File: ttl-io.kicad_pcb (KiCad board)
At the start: 4 copper layers, 47.2 x 30 mm, 56 parts, among them J1 PMOD, J2 430451628, U1 SN74LVC1G16DBVR, U2 SN74LVC1G16DBVR, U3 SN74LVC1G16DBVR, U4 SN74LVC1G16DBVR, U5 SN74AC14PWR, U6 SN74LVC3G34DCT, U7 SN74LVC3G34DCT, U8 SN74LVC3G34DCT, U9 SN74LVC3G34DCT

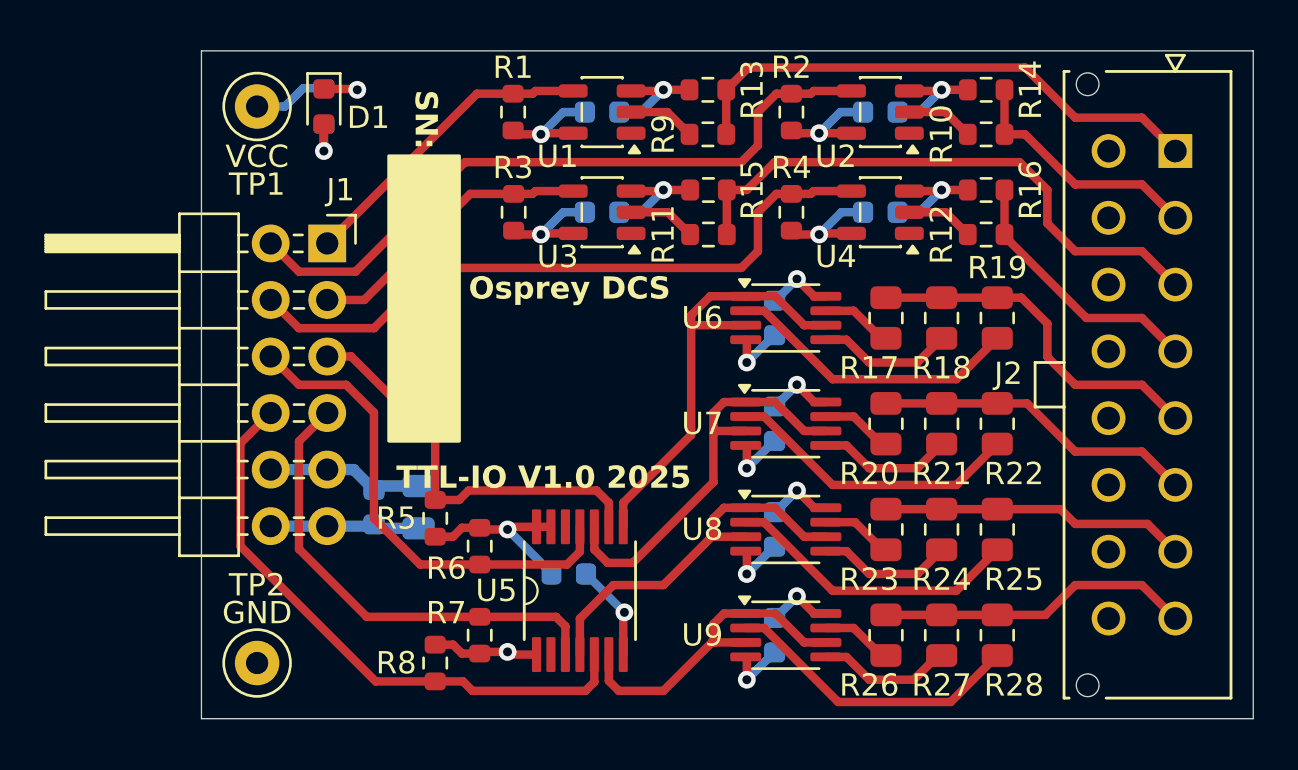
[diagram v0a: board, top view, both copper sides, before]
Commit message: pcb tweaks, date/ver, U5 3D model, 0.4mm holes
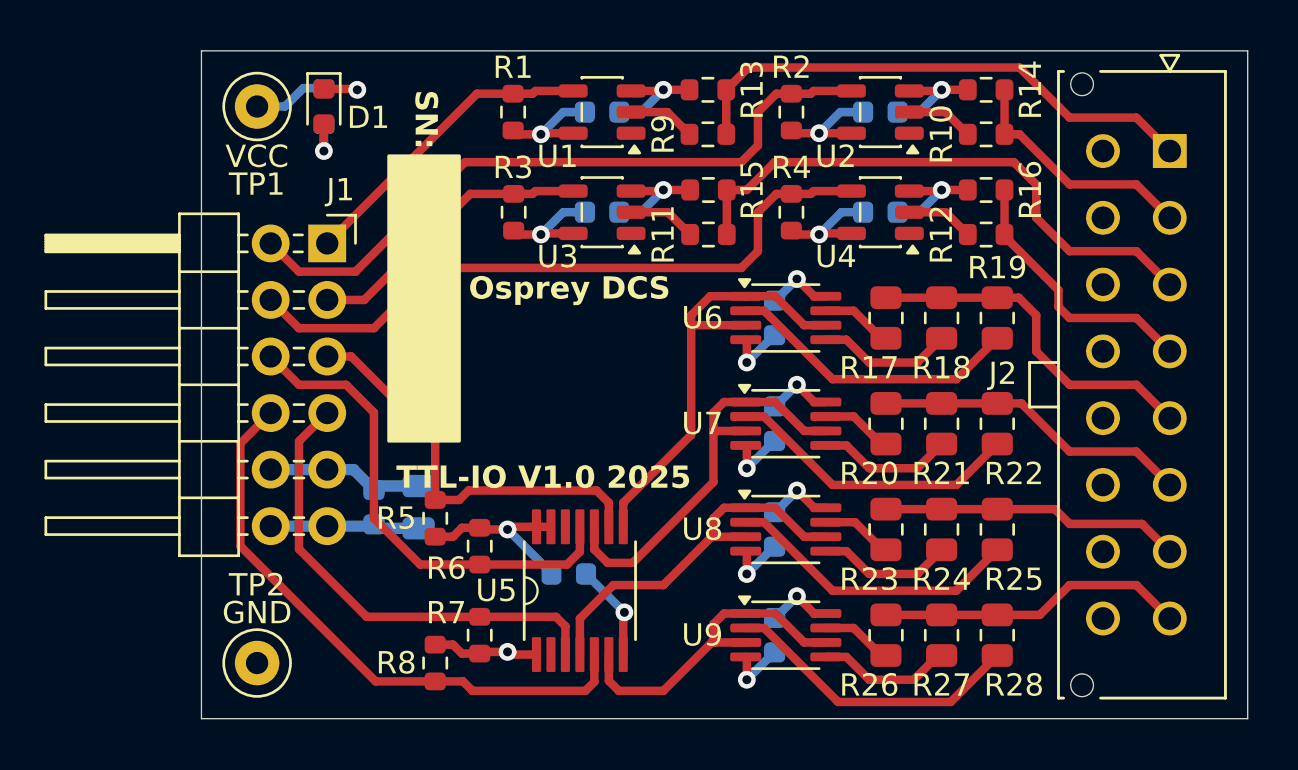
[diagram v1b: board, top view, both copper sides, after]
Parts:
- moved J2 0.25 mm to (169.5, 85.0)
- moved Logo1 0.25 mm to (160.9, 85.6)
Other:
- board size 47.2 x 30 mm -> 47 x 30 mm

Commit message: 30x35mm version initial commit
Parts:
- removed J2: 430451628, 0local:430451628
- removed the R17 at (158.2, 82.0)
- removed the R18 at (160.8, 82.0)
- removed the R19 at (163.2, 82.0)
- removed the R20 at (158.2, 86.8)
- removed the R21 at (160.8, 86.8)
- removed the R22 at (163.2, 86.8)
- removed the R23 at (158.2, 91.5)
- removed the R24 at (160.8, 91.5)
- removed the R25 at (163.2, 91.5)
- removed the R26 at (158.2, 96.2)
- removed the R27 at (160.8, 96.2)
- removed the R28 at (163.2, 96.2)
- added I1: MMCX, 0local:MMCX_THT_Vertical, F.Cu at (154.2, 72.8)
- added I2: MMCX, 0local:MMCX_THT_Vertical, F.Cu at (154.2, 79.8)
- added I3: MMCX, 0local:MMCX_THT_Vertical, F.Cu at (154.2, 86.7)
- added I4: MMCX, 0local:MMCX_THT_Vertical, F.Cu at (154.2, 93.8)
- added O1: MMCX, 0local:MMCX_THT_Vertical, F.Cu at (159.8, 76.2)
- added O2: MMCX, 0local:MMCX_THT_Vertical, F.Cu at (159.8, 83.2)
- added O3: MMCX, 0local:MMCX_THT_Vertical, F.Cu at (159.8, 90.2)
- added O4: MMCX, 0local:MMCX_THT_Vertical, F.Cu at (159.8, 97.2)
- added R10: 10, 0local:R_0805_2012Metric, F.Cu at (149.8, 81.2)
- added R11: 10, 0local:R_0805_2012Metric, F.Cu at (149.8, 88.8)
- added R12: 10, 0local:R_0805_2012Metric, F.Cu at (149.8, 90.8)
- added R13: 10, 0local:R_0805_2012Metric, F.Cu at (149.8, 92.8)
- added R14: 10, 0local:R_0805_2012Metric, F.Cu at (149.8, 94.8)
- added R15: 10, 0local:R_0805_2012Metric, F.Cu at (149.8, 96.8)
- added R16: 10, 0local:R_0805_2012Metric, F.Cu at (149.8, 98.8)
- added R5: 10, 0local:R_0805_2012Metric, F.Cu at (149.8, 71.2)
- added R6: 10, 0local:R_0805_2012Metric, F.Cu at (149.8, 73.2)
- added R7: 10, 0local:R_0805_2012Metric, F.Cu at (149.8, 75.2)
- added R8: 10, 0local:R_0805_2012Metric, F.Cu at (149.8, 77.2)
- added R9: 10, 0local:R_0805_2012Metric, F.Cu at (149.8, 79.2)
- C1, C2, C3, C4: moved to F.Cu
- R17: renamed from R13; moved to B.Cu
- R18: renamed from R14; moved to B.Cu
- R19: renamed from R15; moved to B.Cu
- R20: renamed from R16; moved to B.Cu
- R21: renamed from R9; moved to B.Cu
- R22: renamed from R10; moved to B.Cu
- R23: renamed from R11; moved to B.Cu
- R24: renamed from R12; moved to B.Cu
- R25: renamed from R1; moved to B.Cu
- R26: renamed from R2; moved to B.Cu
- R27: renamed from R3; moved to B.Cu
- R28: renamed from R4; moved to B.Cu
- U6: renamed from U1; moved to B.Cu
- U7: renamed from U2; moved to B.Cu
- U8: renamed from U3; moved to B.Cu
- U9: renamed from U4; moved to B.Cu
- moved C4 27.2 mm to (139.2, 97.0), turned to 90 degrees
- moved U9 27.2 mm to (139.2, 97.0)
- moved R28 26.7 mm to (136.0, 97.0), turned to -90 degrees
- moved R20 21.7 mm to (151.0, 94.5), turned to 90 degrees
- moved R24 21.2 mm to (148.2, 93.8)
- moved C2 19.3 mm to (139.2, 77.5), turned to 90 degrees
- moved U7 19.3 mm to (139.2, 77.5)
- moved R26 18.6 mm to (136.0, 77.5), turned to -90 degrees
- moved R27 17.5 mm to (135.0, 93.5), turned to 0 degrees
- moved C3 16.5 mm to (139.2, 92.5), turned to 90 degrees
- moved U8 16.5 mm to (139.2, 92.5)
- moved R22 15.7 mm to (148.2, 79.8)
- moved C9 15.3 mm to (136.8, 80.0)
- moved R19 14.8 mm to (155.0, 90.2), turned to 180 degrees
- moved R18 13.8 mm to (151.0, 79.0), turned to -90 degrees
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- renumbered C6 to C5, C7 to C6, C8 to C7, C9 to C8, C5 to C9, R5 to R1, R6 to R2, R7 to R3, R8 to R4, U5 to U1, U6 to U2, U7 to U3, U8 to U4, U9 to U5
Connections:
- U1 pad 1: +3.3V -> /PMOD_OUT4
- U1 pad 10: Net-(U5-5Y) -> Net-(U1-5Y)
- U1 pad 11: /PMOD_OUT2 -> /PMOD_OUT1
- U1 pad 2: unconnected-(U5-1Y-Pad2) -> Net-(U1-1Y)
- U1 pad 3: /PMOD_OUT3 -> +3.3V
- U1 pad 4: Net-(U5-2Y) (its old number) -> unconnected-(U1-2Y-Pad4)
- U1 pad 5: /PMOD_OUT4 -> /PMOD_OUT3
- U1 pad 6: Net-(U5-3Y) (its old number) -> Net-(U1-3Y)
- U1 pad 8: Net-(U5-4Y) -> Net-(U1-4Y)
- U1 pad 9: /PMOD_OUT1 -> /PMOD_OUT2
- U2 pad 1: Net-(U5-4Y) -> Net-(U1-5Y)
- U2 pad 3: Net-(U5-4Y) -> Net-(U1-5Y)
- U2 pad 6: Net-(U5-4Y) -> Net-(U1-5Y)
- U3 pad 1: Net-(U5-5Y) -> Net-(U1-4Y)
- U3 pad 3: Net-(U5-5Y) -> Net-(U1-4Y)
- U3 pad 6: Net-(U5-5Y) -> Net-(U1-4Y)
- U4 pad 1: Net-(U5-2Y) (its old number) -> Net-(U1-3Y)
- U4 pad 3: Net-(U5-2Y) (its old number) -> Net-(U1-3Y)
- U4 pad 6: Net-(U5-2Y) (its old number) -> Net-(U1-3Y)
- U5 pad 1: Net-(U5-3Y) (its old number) -> Net-(U1-1Y)
- U5 pad 3: Net-(U5-3Y) (its old number) -> Net-(U1-1Y)
- U5 pad 6: Net-(U5-3Y) (its old number) -> Net-(U1-1Y)
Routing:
- net /PMOD_IN2: track 30.9 -> 8.59 mm
- net /IN3: track 25.6 -> 5.14 mm
- net Net-(U5-4Y): track 20.2 -> 0.00 mm
- net /IN1: track 23.9 -> 5.24 mm
- net Net-(U5-5Y): track 18.5 -> 0.00 mm
- net Net-(U1-5Y): track 0.00 -> 18.3 mm
- net Net-(U1-1Y): track 0.00 -> 18.0 mm
- net /PMOD_OUT4: track 26.5 -> 8.82 mm
- net Net-(U5-2Y) (its old number): track 17.1 -> 0.00 mm
- net Net-(U5-3Y) (its old number): track 15.1 -> 0.00 mm
- net Net-(U1-4Y): track 0.00 -> 12.3 mm
- net Net-(U1-3Y): track 0.00 -> 12.0 mm
- net /PMOD_OUT1: track 18.4 -> 8.83 mm
- net /PMOD_OUT3: track 21.3 -> 12.6 mm
- net /PMOD_IN4: track 30.2 -> 21.6 mm
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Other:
- board size 47 x 30 mm -> 35 x 30 mm
- board text added: "Osprey TTL-IO V1.0 2025"
- board text removed: "Osprey DCS"
- board text removed: "TTL-IO V1.0 2025"

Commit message: swapped I/O MMCX columns
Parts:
- moved I3 6.55 mm to (159.8, 90.2)
- moved I1 6.52 mm to (159.8, 76.2)
- moved I2 6.52 mm to (159.8, 83.2)
- moved I4 6.52 mm to (159.8, 97.2)
- moved O1 6.52 mm to (154.2, 72.8)
- moved O2 6.52 mm to (154.2, 79.8)
- moved O3 6.52 mm to (154.2, 86.8)
- moved O4 6.52 mm to (154.2, 93.8)
- moved R19 4.12 mm to (151.0, 91.2), turned to 90 degrees
- moved R21 3.51 mm to (148.0, 76.2)
- moved R23 3.51 mm to (148.2, 90.5)
- moved R24 3.25 mm to (148.2, 97.0)
- moved R17 2.02 mm to (150.8, 75.5), turned to -90 degrees
- moved R20 1.75 mm to (151.0, 96.2), turned to -90 degrees
- moved R18 0.56 mm to (150.8, 79.5)
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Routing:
- net /IN2: track 5.37 -> 12.3 mm
- net /OUT2: track 14.0 -> 7.94 mm
- net /IN1: track 5.24 -> 11.0 mm
- net /IN3: track 5.14 -> 10.8 mm
- net /OUT1: track 13.5 -> 7.94 mm
- net /IN4: track 5.24 -> 10.8 mm
- net /OUT4: track 13.3 -> 8.10 mm
- net /OUT3: track 13.3 -> 8.51 mm
- net Net-(U8-1A): track 11.3 -> 7.70 mm
- net Net-(U6-1A): track 8.47 -> 9.60 mm

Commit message: slotted mounting hole
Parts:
- removed Logo1: Logo_Open_Hardware_Small, 0local:Logo_2X
